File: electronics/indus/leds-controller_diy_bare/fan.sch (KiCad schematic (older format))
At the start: 4 parts

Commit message: wip bare diy controller - dcdc and refactor
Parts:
- gave numbers to parts that had none: 4
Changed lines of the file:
@@
 $Descr A4 11693 8268
 encoding utf-8
-Sheet 7 8
+Sheet 7 9
 Title "Carte controlleur de LEDs 4 canaux"
 Date ""
@@
 Fan_PWM
 $Comp
-L MOSFET_N Q?
+L MOSFET_N Q1
 U 1 1 57113EAA
 P 6450 3750
-F 0 "Q?" H 6460 3920 60  0000 R CNN
+F 0 "Q1" H 6460 3920 60  0000 R CNN
 F 1 "2N7002" H 6460 3600 60  0000 R CNN
 F 2 "risebox:SOT-23-FET" H 6450 3750 60  0001 C CNN
@@
 $EndComp
 $Comp
-L R-RESCUE-leds-controller R?
+L R-RESCUE-leds-controller R32
 U 1 1 57113EAB
 P 5150 3750
-F 0 "R?" V 5230 3750 40  0000 C CNN
+F 0 "R32" V 5230 3750 40  0000 C CNN
 F 1 "100" V 5157 3751 40  0000 C CNN
 F 2 "Resistors_SMD:R_0603" V 5080 3750 30  0001 C CNN
@@
 $EndComp
 $Comp
-L R-RESCUE-leds-controller R?
+L R-RESCUE-leds-controller R33
 U 1 1 57113EAC
 P 5800 4250
-F 0 "R?" V 5880 4250 40  0000 C CNN
+F 0 "R33" V 5880 4250 40  0000 C CNN
 F 1 "10K" V 5807 4251 40  0000 C CNN
 F 2 "Resistors_SMD:R_0603" V 5730 4250 30  0001 C CNN
@@
 $EndComp
 $Comp
-L DIODE D?
+L DIODE D7
 U 1 1 57113EAD
 P 6900 3100
-F 0 "D?" H 6900 3200 40  0000 C CNN
+F 0 "D7" H 6900 3200 40  0000 C CNN
 F 1 "RS1A DIODE" H 6900 3000 40  0000 C CNN
 F 2 "ab2tech:AB2_DO-214AC" H 6900 3100 60  0001 C CNN
@@
 	6750 4650 5800 4650
 $Comp
-L GND-RESCUE-leds-controller #PWR?
+L GND-RESCUE-leds-controller #PWR024
 U 1 1 57113EAE
 P 5800 5400
-F 0 "#PWR?" H 5800 5400 30  0001 C CNN
+F 0 "#PWR024" H 5800 5400 30  0001 C CNN
 F 1 "GND" H 5800 5330 30  0001 C CNN
 F 2 "" H 5800 5400 60  0000 C CNN

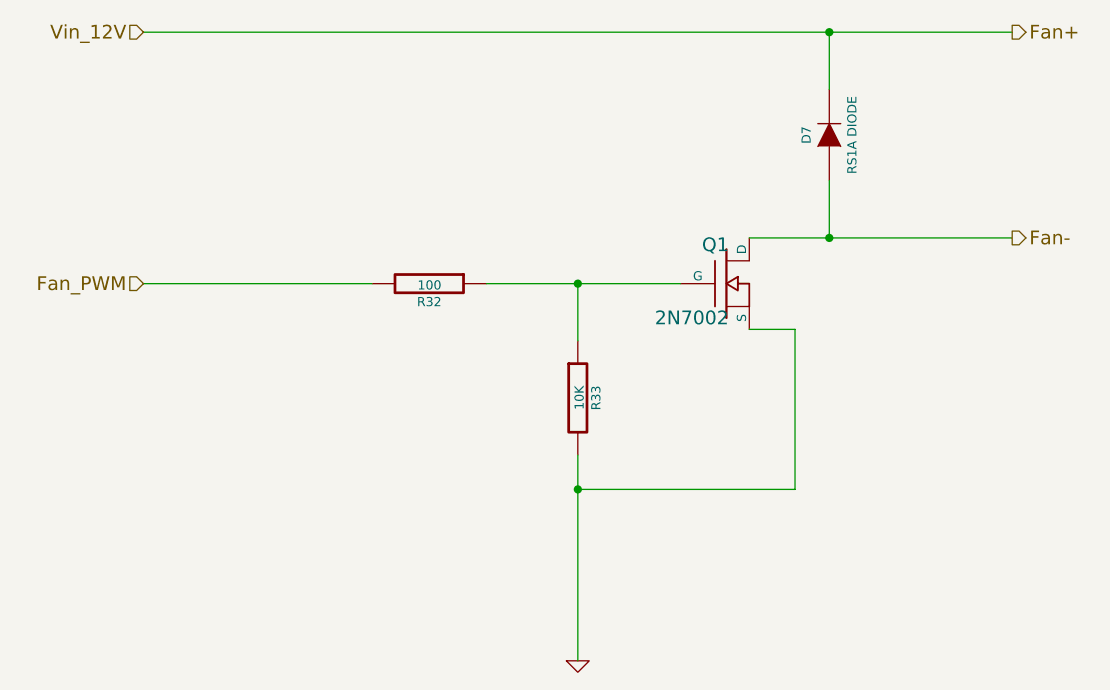
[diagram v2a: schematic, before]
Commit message: schema prctically ok missing refs
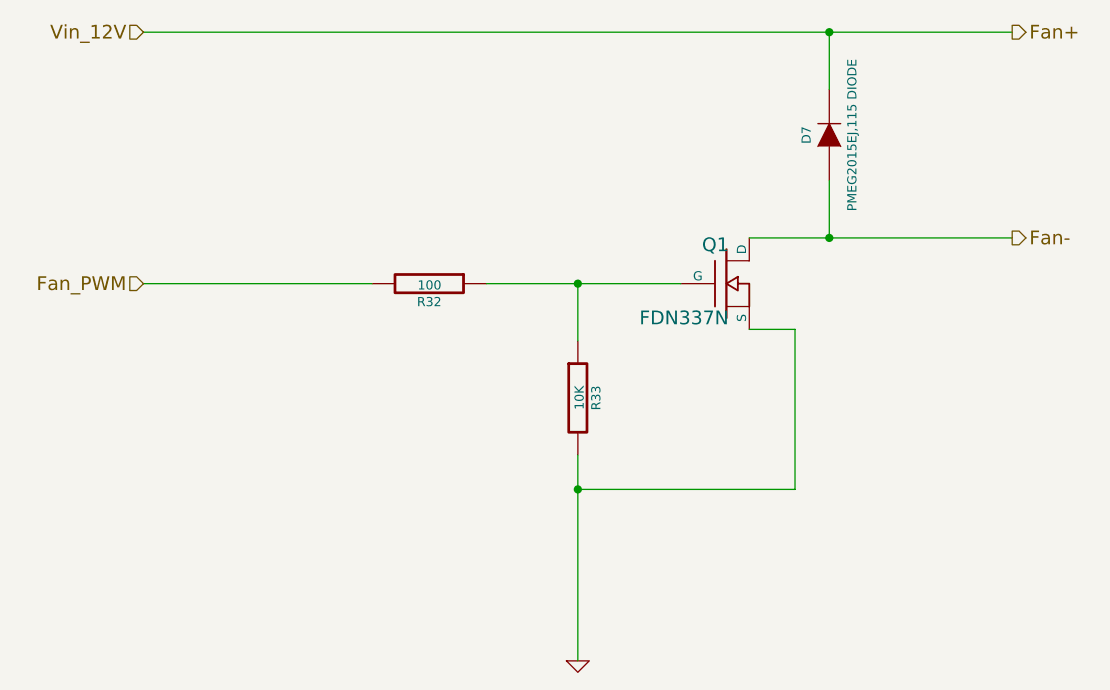
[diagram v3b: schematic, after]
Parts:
- D7: value RS1A DIODE -> PMEG2015EJ,115 DIODE
- Q1: value 2N7002 -> FDN337N
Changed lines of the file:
@@
 $Descr A4 11693 8268
 encoding utf-8
-Sheet 7 9
+Sheet 6 9
 Title "Carte controlleur de LEDs 4 canaux"
 Date ""
@@
 P 6450 3750
 F 0 "Q1" H 6460 3920 60  0000 R CNN
-F 1 "2N7002" H 6460 3600 60  0000 R CNN
+F 1 "FDN337N" H 6460 3600 60  0000 R CNN
 F 2 "risebox:SOT-23-FET" H 6450 3750 60  0001 C CNN
 F 3 "" H 6450 3750 60  0000 C CNN
@@
 P 6900 3100
 F 0 "D7" H 6900 3200 40  0000 C CNN
-F 1 "RS1A DIODE" H 6900 3000 40  0000 C CNN
+F 1 "PMEG2015EJ,115 DIODE" H 6900 3000 40  0000 C CNN
 F 2 "ab2tech:AB2_DO-214AC" H 6900 3100 60  0001 C CNN
 F 3 "" H 6900 3100 60  0000 C CNN

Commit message: bom refs etc
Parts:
- D7: value PMEG2015EJ,115 DIODE -> S1A Multicomp DIODE
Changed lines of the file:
@@
 P 6900 3100
 F 0 "D7" H 6900 3200 40  0000 C CNN
-F 1 "PMEG2015EJ,115 DIODE" H 6900 3000 40  0000 C CNN
+F 1 "S1A Multicomp DIODE" H 6900 3000 40  0000 C CNN
 F 2 "ab2tech:AB2_DO-214AC" H 6900 3100 60  0001 C CNN
 F 3 "" H 6900 3100 60  0000 C CNN

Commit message: footprint with libraries
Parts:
- D7: footprint ab2tech:AB2_DO-214AC -> ab2_passive:AB2_DO-214AC
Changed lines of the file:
@@
 F 0 "D7" H 6900 3200 40  0000 C CNN
 F 1 "S1A Multicomp DIODE" H 6900 3000 40  0000 C CNN
-F 2 "ab2tech:AB2_DO-214AC" H 6900 3100 60  0001 C CNN
+F 2 "ab2_passive:AB2_DO-214AC" H 6900 3100 60  0001 C CNN
 F 3 "" H 6900 3100 60  0000 C CNN
 	1    6900 3100
@@
 	6750 4650 5800 4650
 $Comp
-L GND-RESCUE-leds-controller #PWR15
+L GND-RESCUE-leds-controller #PWR016
 U 1 1 57113EAE
 P 5800 5400
-F 0 "#PWR15" H 5800 5400 30  0001 C CNN
+F 0 "#PWR016" H 5800 5400 30  0001 C CNN
 F 1 "GND" H 5800 5330 30  0001 C CNN
 F 2 "" H 5800 5400 60  0000 C CNN
